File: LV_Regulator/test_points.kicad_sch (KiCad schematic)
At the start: 1 part

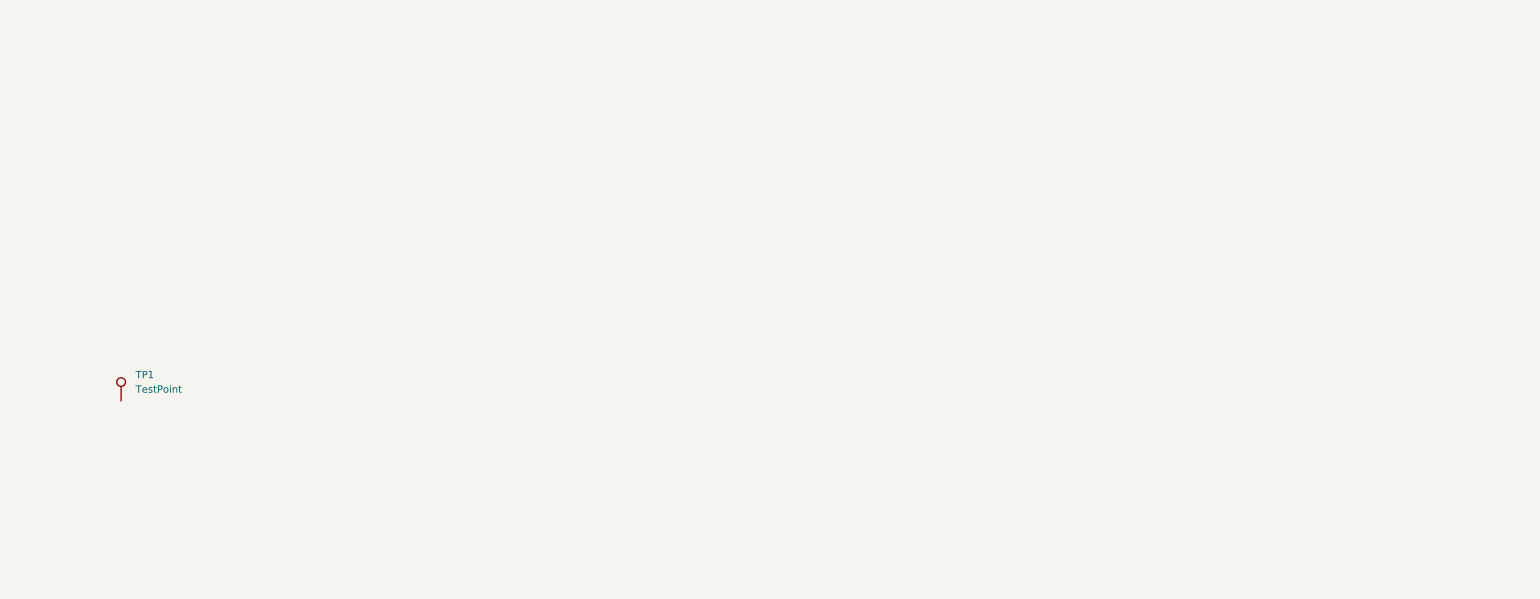
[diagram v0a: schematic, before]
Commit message: Added footprints and Test points
Added test points, yet to connect them have to find where they all go exactly
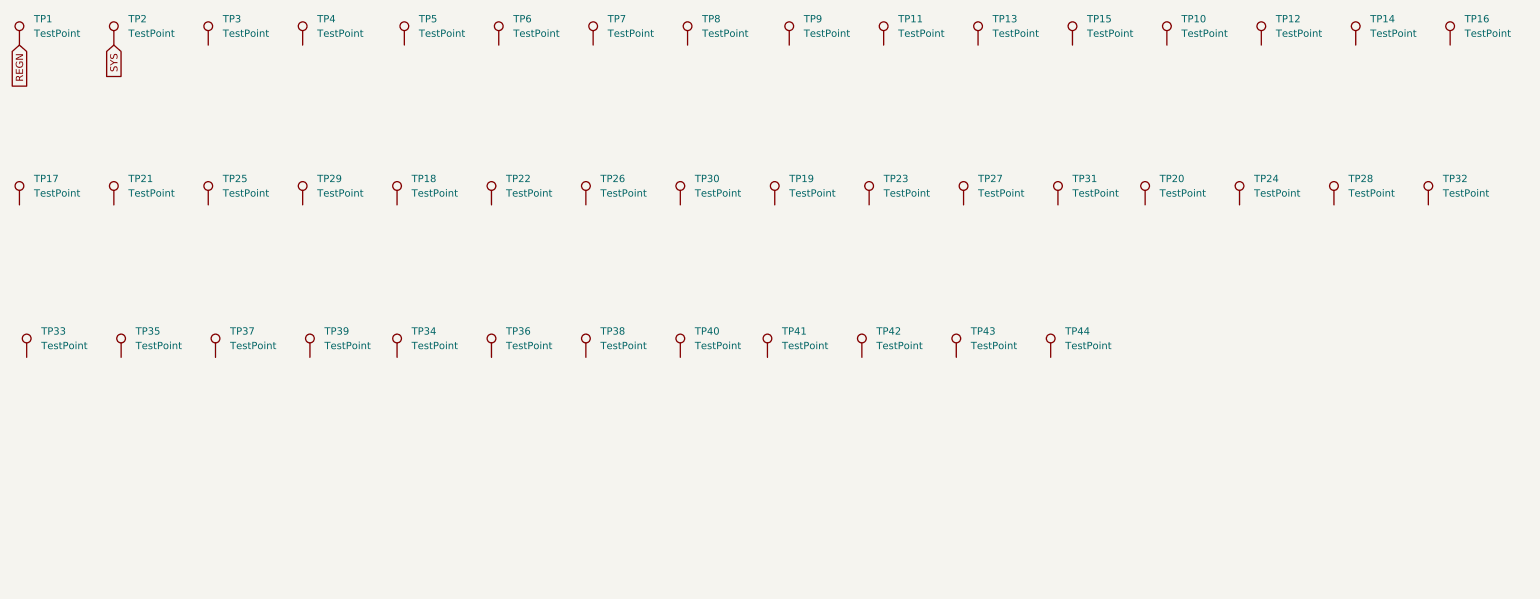
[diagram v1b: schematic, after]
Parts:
- added TP10, TP11, TP12, TP13, TP14, TP15, TP16, TP17, TP18, TP19, TP2, TP20, TP21, TP22, TP23, TP24, TP25, TP26, TP27, TP28, TP29, TP3, TP30, TP31, TP32, TP33, TP34, TP35, TP36, TP37, TP38, TP39, TP4, TP40, TP41, TP42, TP43, TP44, TP5, TP6, TP7, TP8, TP9: TestPoint, TestPoint:TestPoint_Pad_1.0x1.0mm, symbol Connector:TestPoint
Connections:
- net REGN: now reaches TP1.1
- new net SYS: TP2.1
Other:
- moved on the sheet: TP1

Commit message: Halfway Push of adding 3D models to PCB layout components
Pushing with components left to add to finish on main PC
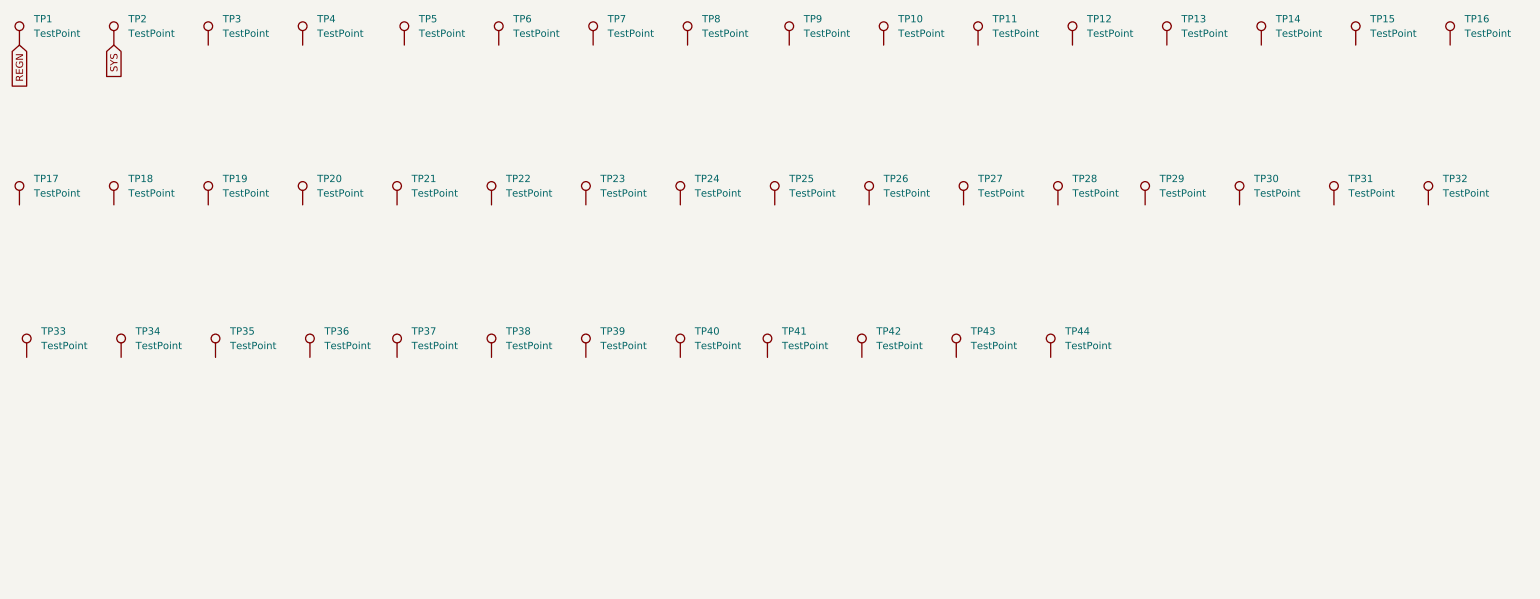
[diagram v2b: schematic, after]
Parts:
- renumbered TP11 to TP10, TP13 to TP11, TP15 to TP12, TP10 to TP13, TP12 to TP14, TP14 to TP15, TP21 to TP18, TP25 to TP19, TP29 to TP20, TP18 to TP21, TP26 to TP23, TP30 to TP24, TP19 to TP25, TP23 to TP26, TP31 to TP28, TP20 to TP29, TP24 to TP30, TP28 to TP31, TP35 to TP34, TP37 to TP35, TP39 to TP36, TP34 to TP37, TP36 to TP38, TP38 to TP39

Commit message: LV Regulator Switching layout Started
Rough placement of components bigger components, a well as giving a capacitor a 3D model it lacked for the 3D View.
More precise placement is in queue and actual PCB routing.
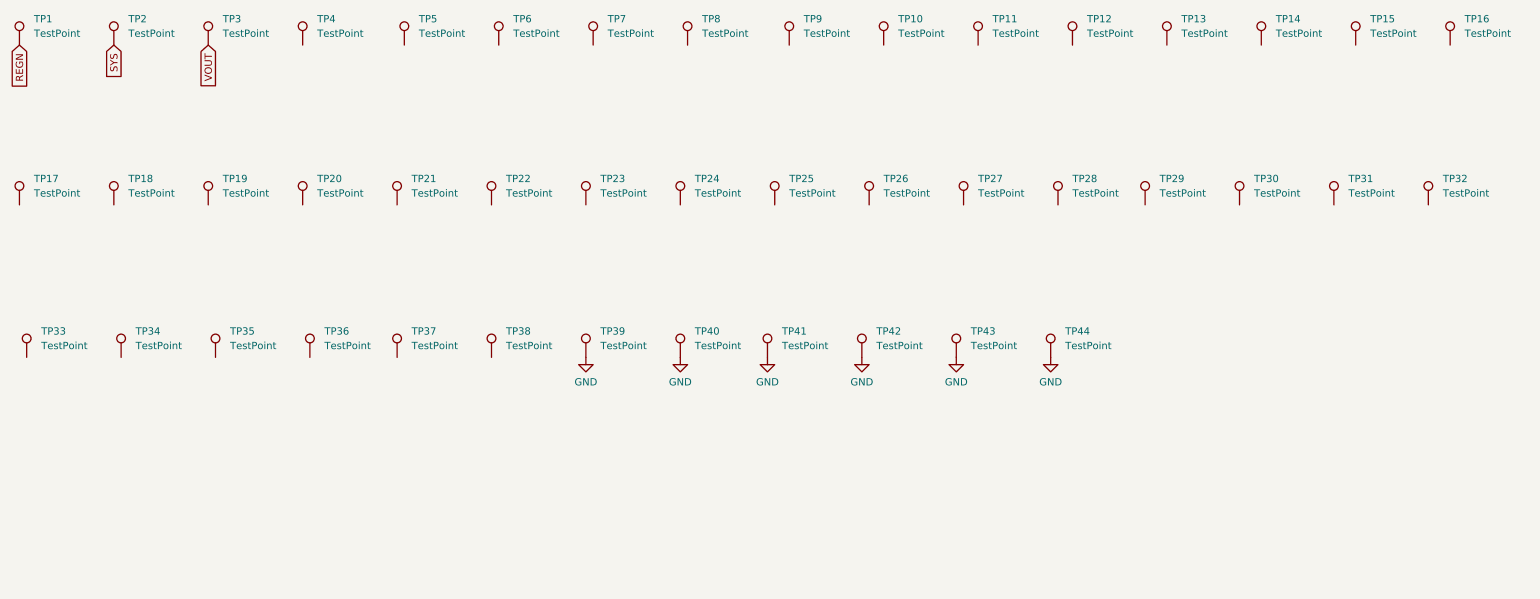
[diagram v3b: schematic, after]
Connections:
- net GND: now reaches TP43.1
- net GND: now also TP39.1, TP40.1, TP41.1, TP42.1, TP44.1
- net VOUT: now reaches TP3.1

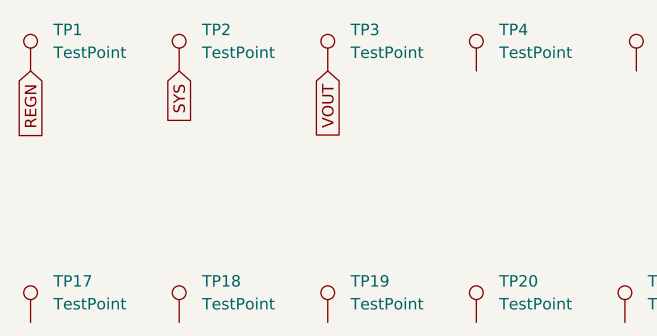
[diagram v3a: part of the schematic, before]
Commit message: Component Placement and Routing
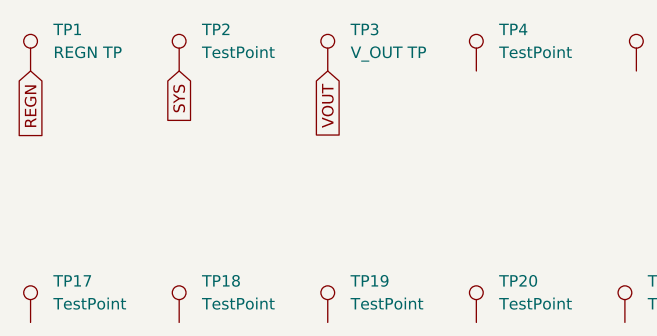
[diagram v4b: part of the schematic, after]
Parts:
- TP1: value TestPoint -> REGN TP
- TP3: value TestPoint -> V_OUT TP
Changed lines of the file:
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@@
 			)
 		)
-		(property "Value" "TestPoint"
+		(property "Value" "V_OUT TP"
 			(at 52.07 18.2879 0)
 			(effects
@@
 			)
 		)
-		(property "Value" "TestPoint"
+		(property "Value" "REGN TP"
 			(at 19.05 18.2879 0)
 			(effects

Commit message: Continued PCB Routing
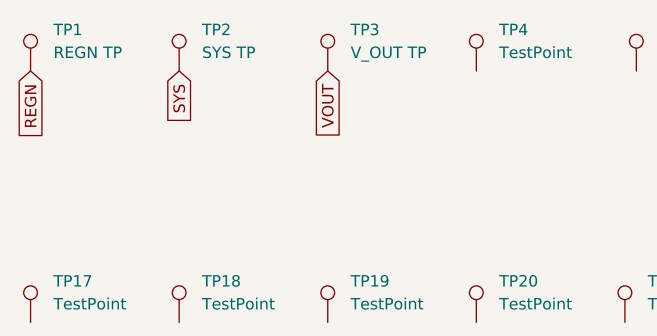
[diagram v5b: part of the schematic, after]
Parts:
- TP2: value TestPoint -> SYS TP
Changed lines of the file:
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@@
 			)
 		)
-		(property "Value" "TestPoint"
+		(property "Value" "SYS TP"
 			(at 35.56 18.2879 0)
 			(effects

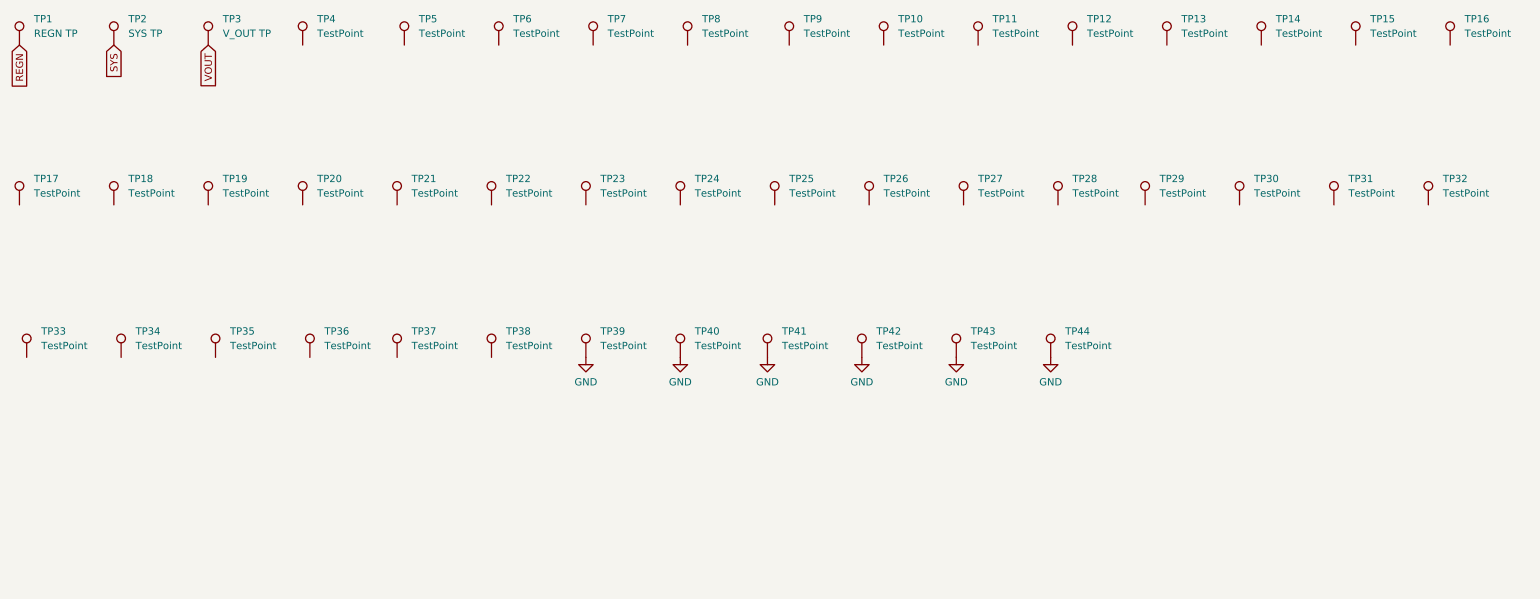
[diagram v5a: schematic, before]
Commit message: PCB routing and TP placement
Finished first PCB routing and started TP placement
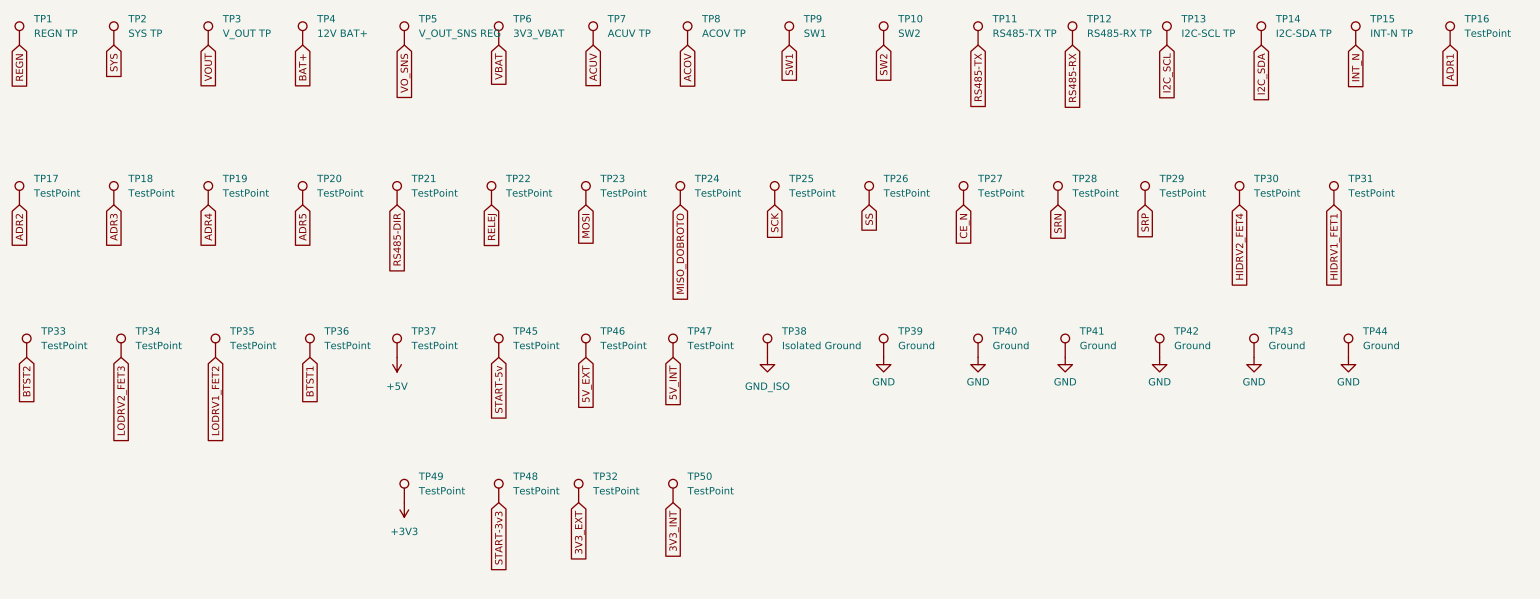
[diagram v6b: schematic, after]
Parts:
- added TP45, TP46, TP47, TP48, TP49, TP50: TestPoint, TestPoint:TestPoint_Pad_1.0x1.0mm, symbol Connector:TestPoint
- TP10: value TestPoint -> SW2
- TP11: value TestPoint -> RS485-TX TP
- TP12: value TestPoint -> RS485-RX TP
- TP13: value TestPoint -> I2C-SCL TP
- TP14: value TestPoint -> I2C-SDA TP
- TP15: value TestPoint -> INT-N TP
- TP38: value TestPoint -> Isolated Ground
- TP39, TP40, TP41, TP42, TP43, TP44: value TestPoint -> Ground
- TP4: value TestPoint -> 12V BAT+
- TP5: value TestPoint -> V_OUT_SNS REG
- TP6: value TestPoint -> 3V3_VBAT
- TP7: value TestPoint -> ACUV TP
- TP8: value TestPoint -> ACOV TP
- TP9: value TestPoint -> SW1
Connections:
- net ACOV: now reaches TP8.1
- net SS: now reaches TP26.1
- net RS485-RX: now reaches TP12.1
- net +5V: now reaches TP37.1
- net RS485-TX: now reaches TP11.1
- net SW1: now reaches TP9.1
- net CE_N: now reaches TP27.1
- net BTST1: now reaches TP36.1
- net ADR5: now reaches TP20.1
- net SW2: now reaches TP10.1
- net SRP: now reaches TP29.1
- net INT_N: now reaches TP15.1
- net HIDRV1_FET1: now reaches TP31.1
- net I2C_SCL: now reaches TP13.1
- net ADR4: now reaches TP19.1
- net I2C_SDA: now reaches TP14.1
- net VO_SNS: now reaches TP5.1
- net BAT+: now reaches TP4.1
- net BTST2: now reaches TP33.1
- net ADR3: now reaches TP18.1
- net GND_ISO: now reaches TP38.1
- net MOSI: now reaches TP23.1
- net ADR2: now reaches TP17.1
- net SCK: now reaches TP25.1
- net ACUV: now reaches TP7.1
- net LODRV2_FET3: now reaches TP34.1
- net RELEJ: now reaches TP22.1
- net SRN: now reaches TP28.1
- net ADR1: now reaches TP16.1
- net 3V3_EXT: now reaches TP32.1
- net MISO_DOBROTO: now reaches TP24.1
- net RS485-DIR: now reaches TP21.1
- net HIDRV2_FET4: now reaches TP30.1
- net VBAT: now reaches TP6.1
- net LODRV1_FET2: now reaches TP35.1
- new net +3V3: TP49.1
- new net 3V3_INT: TP50.1
- new net 5V_EXT: TP46.1
- new net 5V_INT: TP47.1
- new net START-3v3: TP48.1
- new net START-5v: TP45.1
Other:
- moved on the sheet: TP32, TP38, TP39, TP40, TP41, TP42, TP43, TP44

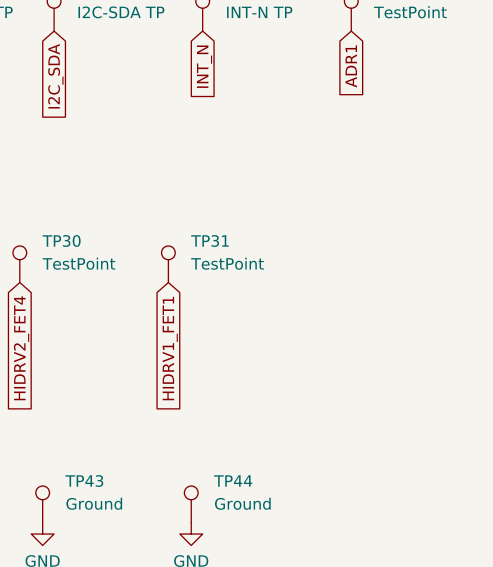
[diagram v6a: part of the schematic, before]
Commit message: Deleted Draft Regulator and Test Points Routing
Deleted Draft Routing of the Regulator and Power Electronics side of the board, because layout was not optimal in the slightest, & will replace and re-route the whole power electronics side.
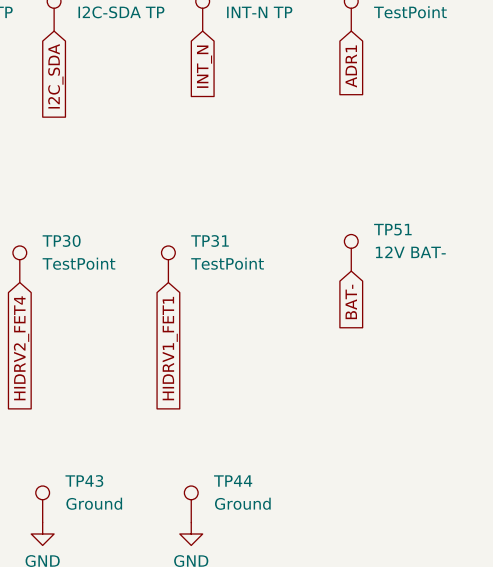
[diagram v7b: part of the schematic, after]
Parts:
- added TP51: 12V BAT-, TestPoint:TestPoint_Pad_1.0x1.0mm, symbol Connector:TestPoint
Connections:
- new net BAT-: TP51.1
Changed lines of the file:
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@@
+		)
+	)
+	(global_label "BAT-"
+		(shape input)
+		(at 266.7 46.99 270)
+		(fields_autoplaced yes)
+		(effects
+			(font
+				(size 1.27 1.27)
+			)
+			(justify right)
+		)
+		(property "Intersheetrefs" "${INTERSHEET_REFS}"
+			(at 266.7 54.8738 90)
+			(effects
+				(font
+					(size 1.27 1.27)
+				)
+				(justify right)
+				(hide yes)
+			)
 		)
 	)
@@
 					(unit 1)
 				)
+			)
+		)
+	)
+	(symbol
+		(lib_id "Connector:TestPoint")
+		(at 266.7 46.99 0)
+		(unit 1)
+		(exclude_from_sim no)
+		(in_bom yes)
+		(on_board yes)
+		(dnp no)
+		(fields_autoplaced yes)
+		(property "Reference" "TP51"
+			(at 269.24 42.4179 0)
+			(effects
+				(font
+					(size 1.27 1.27)
+				)
+				(justify left)
+			)
+		)
+		(property "Value" "12V BAT-"
+			(at 269.24 44.9579 0)
+			(effects
+				(font
+					(size 1.27 1.27)
+				)
+				(justify left)
+			)
+		)
+		(property "Footprint" "TestPoint:TestPoint_Pad_1.0x1.0mm"
+			(at 271.78 46.99 0)
+			(effects
+				(font
+					(size 1.27 1.27)
+				)
+				(hide yes)
+			)
+		)
+		(property "Datasheet" "~"
+			(at 271.78 46.99 0)
+			(effects
+				(font
+					(size 1.27 1.27)
+				)
+				(hide yes)
+			)
+		)
+		(property "Description" "test point"
+			(at 266.7 46.99 0)
+			(effects
+				(font
+					(size 1.27 1.27)
+				)
+				(hide yes)
+			)
+		)
+		(pin "1"
+		)
+		(instances
+			(project "LV_Regulator"
+				(path "/9003ce10-3354-47c9-924a-fd038a206791/2a3b4c6a-4fff-4003-b38d-0d614227feaf"
+					(reference "TP51")
+					(unit 1)
+				)
